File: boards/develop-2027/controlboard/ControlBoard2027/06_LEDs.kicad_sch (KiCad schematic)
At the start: 12 parts, among them U7 74AHCT125

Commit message: changes
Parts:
- added C51: 22uF, symbol Device:C
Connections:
- net +5V: now also C51.1
- net GND: now also C51.2
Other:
- note added: "LEVEL SHIFTER vs DOTSTAR RATE - checked, it works (design review asked). U7 = SN74AHCT125 quad buffer, tpd ~6-10 ns at 5V, rated well past 100 MHz. The design doc prescales the DotStar SPI to 7.815 Mbit/s (12 MHz is the APA102 ceiling). one bit at 7.815 MHz = 128 ns tpd 10 ns = 8% of a bit -> nowhere near the limit. VERDICT: fine. 3.3V INPUT SIDE - why the part is AHCT, not AHC: AHCT has TTL inpu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"

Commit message: post design review changes
post design review changes
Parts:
- added R66, R67: 100k, symbol Device:R
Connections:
- net GND: now also R66.2, R67.2
- net LED_SPI_MOSI: now also R67.1
- net LED_SPI_SCK: now also R66.1
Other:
- note added: "DOTSTAR LEVEL SHIFT U7 SN74AHCT125 on +5V, 3.3V in -> 5V out, tpd 6-10ns. BB-2020BGR-TRB VIH = 0.7 x VDD = 3.5V, so a shifter is needed. LED SPI (SPI2, TX only) = 3 Mbit/s in V0.3: bit = 333ns, tpd = 3% of a bit. LED max clock under 10MHz. Must be AHCT: VIH 2.0V (TTL). AHC needs 3.5V. Used: 1A p2 -> 1Y p3 CKI, 2A p5 -> 2Y p6 SDI, 1OE/2OE p1/p4 = GND. Spare gates 3/4: inputs p9/p12 = GND, OE p10/p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"
- note added: "ROUTING - DOTSTARS U7 -> D3 CLK/DATA short and routed together, over GND. LED-to-LED CO->CI and DO->DI as matched pairs. C40-C44 at each LED VDD pin. C51 where +5V enters the chain. LEDs in the 5-dot shell pattern."
- note removed: "LEVEL SHIFTER vs DOTSTAR RATE - checked, it works (design review asked). U7 = SN74AHCT125 quad buffer, tpd ~6-10 ns at 5V, rated well past 100 MHz. The design doc prescales the DotStar SPI to 7.815 Mbit/s (12 MHz is the APA102 ceiling). one bit at 7.815 MHz = 128 ns tpd 10 ns = 8% of a bit -> nowhere near the limit. VERDICT: fine. 3.3V INPUT SIDE - why the part is AHCT, not AHC: AHCT has TTL inpu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"

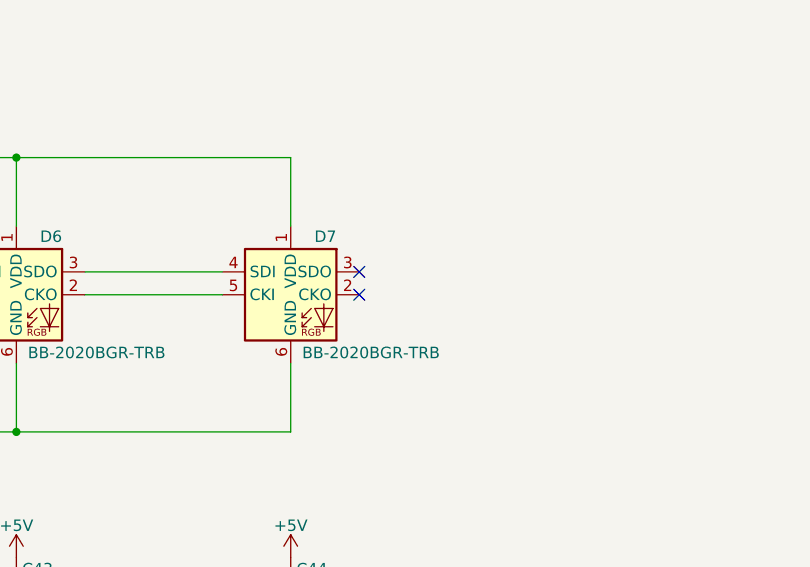
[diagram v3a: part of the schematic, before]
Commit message: added comments. Grouped submodules in ways that make more sense
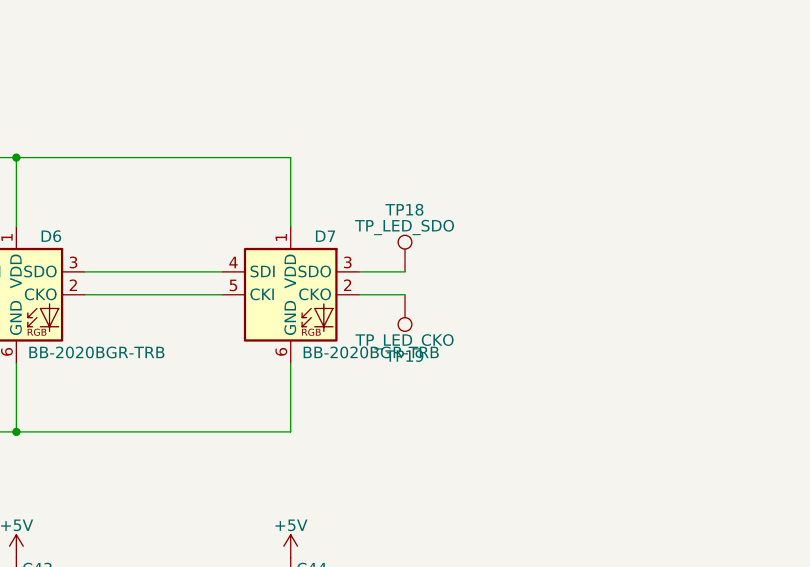
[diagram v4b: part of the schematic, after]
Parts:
- added TP18: TP_LED_SDO, symbol Connector:TestPoint
- added TP19: TP_LED_CKO, symbol Connector:TestPoint
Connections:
- net at D7.2 (CKO): now also TP19.1
- net at D7.3 (SDO): now also TP18.1
- no-connect marks 4 -> 2

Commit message: fixed minor errors
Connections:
- net +5V renamed +5V_PB
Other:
- note added: "DOTSTAR LEVEL SHIFT Power: +5V_PB (powerboard only). The LEDs and U7 are unpowered on USB, so a USB-only board never carries LED current. U7 inputs are rated -0.5 to 7V regardless of VCC and leak +/-1uA at VCC = 0V (SCLS264R), so 3.3V MCU drive is safe while U7 is off. U7 SN74AHCT125, 3.3V in -> 5V out, tpd 6.5ns max at 15pF (SCLS264R). BB-2020BGR-TRB VIH = 0.7 x VDD = 3.5V, so a shifter is neede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"
- note added: "ROUTING - DOTSTARS U7 -> D3 CLK/DATA short and routed together, over GND. LED-to-LED CO->CI and DO->DI as matched pairs. C40-C44 at each LED VDD pin. C51 where +5V_PB enters the chain. LEDs in the 5-dot shell pattern."
- note removed: "DOTSTAR LEVEL SHIFT U7 SN74AHCT125 on +5V, 3.3V in -> 5V out, tpd 6-10ns. BB-2020BGR-TRB VIH = 0.7 x VDD = 3.5V, so a shifter is needed. LED SPI (SPI2, TX only) = 3 Mbit/s in V0.3: bit = 333ns, tpd = 3% of a bit. LED max clock under 10MHz. Must be AHCT: VIH 2.0V (TTL). AHC needs 3.5V. Used: 1A p2 -> 1Y p3 CKI, 2A p5 -> 2Y p6 SDI, 1OE/2OE p1/p4 = GND. Spare gates 3/4: inputs p9/p12 = GND, OE p10/p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"
- note removed: "ROUTING - DOTSTARS U7 -> D3 CLK/DATA short and routed together, over GND. LED-to-LED CO->CI and DO->DI as matched pairs. C40-C44 at each LED VDD pin. C51 where +5V enters the chain. LEDs in the 5-dot shell pattern."

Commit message: Updated comments. Claude did an audit. Take it with huge grains of salt
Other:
- note added: "DOTSTAR LEVEL SHIFT The LEDs need a 5V-level logic high, so U7 (AHCT, TTL inputs) shifts the 3.3V SPI. Powered from +5V_PB: the LEDs never load USB, and U7 inputs are safe while unpowered. Used: 1A p2 -> 1Y p3 CKI, 2A p5 -> 2Y p6 SDI, 1OE/2OE p1/p4 = GND. Spare gates 3/4: inputs p9/p12 = GND, OE p10/p13 = +5V_PB (off), outputs p8/p11 open. R66/R67 hold the inputs low while the MCU pins float at r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"
- note removed: "DOTSTAR LEVEL SHIFT Power: +5V_PB (powerboard only). The LEDs and U7 are unpowered on USB, so a USB-only board never carries LED current. U7 inputs are rated -0.5 to 7V regardless of VCC and leak +/-1uA at VCC = 0V (SCLS264R), so 3.3V MCU drive is safe while U7 is off. U7 SN74AHCT125, 3.3V in -> 5V out, tpd 6.5ns max at 15pF (SCLS264R). BB-2020BGR-TRB VIH = 0.7 x VDD = 3.5V, so a shifter is neede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"
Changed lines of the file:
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@@
     (effects (font (size 1.27 1.27) (bold yes) (color 255 0 0 1)) (justify left bottom))
   )
-  (text "DOTSTAR LEVEL SHIFT\nPower: +5V_PB (powerboard only). The LEDs and U7 are unpowered on USB, so a USB-only\n  board never carries LED current. U7 inputs are rated -0.5 to 7V regardless of VCC and\n  leak +/-1uA at VCC = 0V (SCLS264R), so 3.3V MCU drive is safe while U7 is off.\nU7 SN74AHCT125, 3.3V in -> 5V out, tpd 6.5ns max at 15pF (SCLS264R).\nBB-2020BGR-TRB VIH = 0.7 x VDD = 3.5V, so a shifter is needed.\nLED SPI (SPI2, TX only) = 3 Mbit/s in V0.3:\n   bit = 333ns, tpd = 2% of a bit. LED clock 15MHz abs, under 10MHz operating (p6).\nMust be AHCT: VIH 2.0V (TTL). AHC needs 3.5V.\nUsed: 1A p2 -> 1Y p3 CKI, 2A p5 -> 2Y p6 SDI, 1OE/2OE p1/p4 = GND.\nSpare gates 3/4: inputs p9/p12 = GND, OE p10/p13 = +5V_PB (off), outputs p8/p11 open.\nLED power-on state is not specified: firmware sends an all-off frame first.\n!! Default KiCad APA102-2020 footprint does NOT fit this LED -\n   make one from the BB-2020BGR-TRB land pattern.\n\nDECOUPLING\n   C45 100nF at U7.\n   C40-C44 100nF, one per LED (D3-D7).\n   C51 22uF bulk, >= 10V X5R/X7R. Up to 0.5W per LED (p3): 500mA for 5 LEDs."
+  (text "DOTSTAR LEVEL SHIFT\nThe LEDs need a 5V-level logic high, so U7 (AHCT, TTL inputs) shifts the 3.3V SPI.\nPowered from +5V_PB: the LEDs never load USB, and U7 inputs are safe while unpowered.\nUsed: 1A p2 -> 1Y p3 CKI, 2A p5 -> 2Y p6 SDI, 1OE/2OE p1/p4 = GND.\nSpare gates 3/4: inputs p9/p12 = GND, OE p10/p13 = +5V_PB (off), outputs p8/p11 open.\nR66/R67 hold the inputs low while the MCU pins float at reset.\nLED power-on state is undefined: firmware sends an all-off frame first.\n!! Default KiCad APA102-2020 footprint does NOT fit this LED (C1).\nC45 at U7, C40-C44 one per LED, C51 bulk where +5V_PB enters.\nDESIGN_NOTES.md §10."
     (at 297.18 252.73 0)
     (effects (font (size 1.27 1.27)) (justify left bottom))

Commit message: boxing goes brrr
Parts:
- U7: MPN (none) -> TI SN74AHCT125PWR
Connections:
- net +5V_PB renamed +5V
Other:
- note added: "DOTSTAR CHAIN D3-D7 AND DECOUPLING"
- note added: "DOTSTAR LEVEL SHIFT The LEDs need a 5V-level logic high, so U7 (AHCT, TTL inputs) shifts the 3.3V SPI. LEDs and U7 run from +5V (mux output), so they also work on USB. Firmware caps LED current: ~250mA on the powerboard (F2 budget), ~100mA on USB (F1). Used: 1A p2 -> 1Y p3 CKI, 2A p5 -> 2Y p6 SDI, 1OE/2OE p1/p4 = GND. Spare gates 3/4: inputs p9/p12 = GND, OE p10/p13 = +5V (off), outputs p8/p11 op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"
- note added: "LEVEL SHIFT U7 (3.3V SPI TO 5V)"
- note added: "ROUTING - DOTSTARS U7 -> D3 CLK/DATA short and routed together, over GND. LED-to-LED CO->CI and DO->DI as matched pairs. C40-C44 at each LED VDD pin. C51 where +5V enters the chain. LEDs in the 5-dot shell pattern."
- note added: "U7 SPARE GATES"
- note removed: "DOTSTAR LEVEL SHIFT The LEDs need a 5V-level logic high, so U7 (AHCT, TTL inputs) shifts the 3.3V SPI. Powered from +5V_PB: the LEDs never load USB, and U7 inputs are safe while unpowered. Used: 1A p2 -> 1Y p3 CKI, 2A p5 -> 2Y p6 SDI, 1OE/2OE p1/p4 = GND. Spare gates 3/4: inputs p9/p12 = GND, OE p10/p13 = +5V_PB (off), outputs p8/p11 open. R66/R67 hold the inputs low while the MCU pins float at r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"
- note removed: "ROUTING - DOTSTARS U7 -> D3 CLK/DATA short and routed together, over GND. LED-to-LED CO->CI and DO->DI as matched pairs. C40-C44 at each LED VDD pin. C51 where +5V_PB enters the chain. LEDs in the 5-dot shell pattern."

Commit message: updated schematics based on feedback
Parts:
- added TP20: LED_SDI_IN, TestPoint:TestPoint_Pad_D1.0mm, symbol Connector:TestPoint
- added TP21: LED_CKI_IN, TestPoint:TestPoint_Pad_D1.0mm, symbol Connector:TestPoint
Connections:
- net at D3.5 (CKI), U7.3: now also TP21.1
- net at D3.4 (SDI), U7.6: now also TP20.1
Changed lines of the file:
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@@
 		(color 0 0 0 0)
 	)
+	(junction
+		(at 137.16 177.8)
+		(diameter 0)
+	)
+	(junction
+		(at 137.16 180.34)
+		(diameter 0)
+	)
 	(no_connect
 		(at 93.98 232.41)
@@
 		)
 	)
+	(text "ROUTING - DOTSTARS\nU7 -> D3 CLK/DATA short and routed together, over GND.\nLED-to-LED CO->CI and DO->DI as matched pairs.\nC40-C44 at each LED VDD pin. C51 where +5V enters the chain.\nLEDs in the 5-dot shell pattern."
+		(at 199.39 149.86 0)
+		(effects
+			(font
+				(size 1.27 1.27)
+				(bold yes)
+				(color 255 0 0 1)
+			)
+			(justify left bottom)
+		)
+	)
+	(text "DOTSTAR LEVEL SHIFT\nThe LEDs need a 5V-level logic high, so U7 (AHCT, TTL inputs) shifts the 3.3V SPI.\nLEDs and U7 run from +5V (mux output), so they also work on USB.\nFirmware caps LED current: ~250mA on the powerboard (F2 budget), ~100mA on USB (F1).\nUsed: 1A p2 -> 1Y p3 CKI, 2A p5 -> 2Y p6 SDI, 1OE/2OE p1/p4 = GND.\nSpare gates 3/4: inputs p9/p12 = GND, OE p10/p13 = +5V (off), outputs p8/p11 open.\nR66/R67 hold the inputs low while the MCU pins float at reset.\nLED power-on state is undefined: firmware sends an all-off frame first.\n!! Default KiCad APA102-2020 footprint does NOT fit this LED (C1).\nC45 at U7, C40-C44 one per LED, C51 bulk where +5V enters.\nDESIGN_NOTES.md §10."
+		(at 297.18 252.73 0)
+		(effects
+			(font
+				(size 1.27 1.27)
+			)
+			(justify left bottom)
+		)
+	)
+	(text "LEVEL SHIFT U7 (3.3V SPI TO 5V)"
+		(at 50.8 95.25 0)
+		(effects
+			(font
+				(size 2 2)
+				(thickness 0.4)
+				(bold yes)
+				(color 0 0 132 1)
+			)
+			(justify left bottom)
+		)
+	)
+	(text "DOTSTAR CHAIN D3-D7 AND DECOUPLING"
+		(at 116.84 139.7 0)
+		(effects
+			(font
+				(size 2 2)
+				(thickness 0.4)
+				(bold yes)
+				(color 0 0 132 1)
+			)
+			(justify left bottom)
+		)
+	)
+	(text "U7 SPARE GATES"
+		(at 40.64 229.87 0)
+		(effects
+			(font
+				(size 2 2)
+				(thickness 0.4)
+				(bold yes)
+				(color 0 0 132 1)
+			)
+			(justify left bottom)
+		)
+	)
 	(hierarchical_label "LED_SPI_MOSI"
 		(shape input)
@@
 		)
 	)
-  (text "ROUTING - DOTSTARS\nU7 -> D3 CLK/DATA short and routed together, over GND.\nLED-to-LED CO->CI and DO->DI as matched pairs.\nC40-C44 at each LED VDD pin. C51 where +5V enters the chain.\nLEDs in the 5-dot shell pattern."
-    (at 199.39 149.86 0)
-    (effects (font (size 1.27 1.27) (bold yes) (color 255 0 0 1)) (justify left bottom))
-  )
-  (text "DOTSTAR LEVEL SHIFT\nThe LEDs need a 5V-level logic high, so U7 (AHCT, TTL inputs) shifts the 3.3V SPI.\nLEDs and U7 run from +5V (mux output), so they also work on USB.\nFirmware caps LED current: ~250mA on the powerboard (F2 budget), ~100mA on USB (F1).\nUsed: 1A p2 -> 1Y p3 CKI, 2A p5 -> 2Y p6 SDI, 1OE/2OE p1/p4 = GND.\nSpare gates 3/4: inputs p9/p12 = GND, OE p10/p13 = +5V (off), outputs p8/p11 open.\nR66/R67 hold the inputs low while the MCU pins float at reset.\nLED power-on state is undefined: firmware sends an all-off frame first.\n!! Default KiCad APA102-2020 footprint does NOT fit this LED (C1).\nC45 at U7, C40-C44 one per LED, C51 bulk where +5V enters.\nDESIGN_NOTES.md §10."
-    (at 297.18 252.73 0)
-    (effects (font (size 1.27 1.27)) (justify left bottom))
-  )
-  (text "LEVEL SHIFT U7 (3.3V SPI TO 5V)"
-    (at 50.8 95.25 0)
-    (effects (font (size 2 2) (thickness 0.4) (bold yes) (color 0 0 132 1)) (justify left bottom))
-  )
-  (text "DOTSTAR CHAIN D3-D7 AND DECOUPLING"
-    (at 116.84 139.7 0)
-    (effects (font (size 2 2) (thickness 0.4) (bold yes) (color 0 0 132 1)) (justify left bottom))
-  )
-  (text "U7 SPARE GATES"
-    (at 40.64 229.87 0)
-    (effects (font (size 2 2) (thickness 0.4) (bold yes) (color 0 0 132 1)) (justify left bottom))
-  )
 	(symbol
 		(lib_id "Device:R")
@@
 			)
 		)
+		(property "MPN" "TI SN74AHCT125PWR"
+			(at 86.36 180.34 0)
+			(hide yes)
+			(effects
+				(font
+					(size 1.27 1.27)
+				)
+			)
+		)
 		(body_style 1)
 		(in_pos_files yes)
@@
 			)
 		)
-		(property "MPN" "TI SN74AHCT125PWR"
-			(at 86.36 180.34 0)
-			(hide yes)
-			(effects
-				(font
-					(size 1.27 1.27)
-				)
-			)
-		))
+	)
 	(symbol
 		(lib_id "74xx:74AHCT125")
@@
 			)
 		)
+		(property "MPN" "TI SN74AHCT125PWR"
+			(at 86.36 157.48 0)
+			(hide yes)
+			(effects
+				(font
+					(size 1.27 1.27)
+				)
+			)
+		)
 		(body_style 1)
 		(in_pos_files yes)
@@
 			)
 		)
-		(property "MPN" "TI SN74AHCT125PWR"
-			(at 86.36 157.48 0)
-			(hide yes)
-			(effects
-				(font
-					(size 1.27 1.27)
-				)
-			)
-		))
+	)
 	(symbol
 		(lib_id "power:GND")
@@
 			)
 		)
+		(property "MPN" "TI SN74AHCT125PWR"
+			(at 86.36 232.41 0)
+			(hide yes)
+			(effects
+				(font
+					(size 1.27 1.27)
+				)
+			)
+		)
 		(body_style 1)
 		(in_pos_files yes)
@@
 			)
 		)
-		(property "MPN" "TI SN74AHCT125PWR"
-			(at 86.36 232.41 0)
-			(hide yes)
-			(effects
-				(font
-					(size 1.27 1.27)
-				)
-			)
-		))
+	)
 	(symbol
 		(lib_id "power:GND")
@@
 			)
 		)
+		(property "MPN" "TI SN74AHCT125PWR"
+			(at 86.36 120.65 0)
+			(hide yes)
+			(effects
+				(font
+					(size 1.27 1.27)
+				)
+			)
+		)
 		(body_style 1)
 		(in_pos_files yes)
@@
 			)
 		)
-		(property "MPN" "TI SN74AHCT125PWR"
-			(at 86.36 120.65 0)
-			(hide yes)
-			(effects
-				(font
-					(size 1.27 1.27)
-				)
-			)
-		))
+	)
 	(symbol
 		(lib_id "Device:C")
@@
 			)
 		)
+		(property "MPN" "TI SN74AHCT125PWR"
+			(at 152.4 232.41 0)
+			(hide yes)
+			(effects
+				(font
+					(size 1.27 1.27)
+				)
+			)
+		)
 		(body_style 1)
 		(in_pos_files yes)
@@
 			)
 		)
-		(property "MPN" "TI SN74AHCT125PWR"
-			(at 152.4 232.41 0)
-			(hide yes)
-			(effects
-				(font
-					(size 1.27 1.27)
-				)
-			)
-		))
+	)
 	(symbol
 		(lib_id "power:GND")
@@
 					(unit 1)
 				)
+			)
+		)
+	)
+	(symbol
+		(lib_id "Connector:TestPoint")
+		(at 137.16 177.8 0)
+		(unit 1)
+		(in_bom yes)
+		(on_board yes)
+		(dnp no)
+		(property "Reference" "TP20"
+			(at 137.16 170.942 0)
+			(effects
+				(font
+					(size 1.27 1.27)
+				)
+			)
+		)
+		(property "Value" "LED_SDI_IN"
+			(at 137.16 172.72 0)
+			(effects
+				(font
+					(size 1.27 1.27)
+				)
+			)
+		)
+		(property "Footprint" "TestPoint:TestPoint_Pad_D1.0mm"
+			(at 137.16 177.8 0)
+			(hide yes)
+			(effects
+				(font
+					(size 1.27 1.27)
+				)
+			)
+		)
+		(property "Datasheet" "https://americanbrightled.com/products/rgb-ic-led-components/"
+			(at 137.16 177.8 0)
+			(hide yes)
+			(effects
+				(font
+					(size 1.27 1.27)
+				)
+			)
+		)
+		(property "Description" "Beginning of LED chain: D3 SDI pin 4 after U7 level shifting. Compare against TP18 (D7 SDO)."
+			(at 137.16 177.8 0)
+			(hide yes)
+			(effects
+				(font
+					(size 1.27 1.27)
+				)
+			)
+		)
+		(instances
+			(project "ControlBoard2027"
+				(path "/2be89789-dd04-494d-960d-2531c7ce8a2f/ee62a278-a94c-4411-ba4b-a0279340f73e"
+					(reference "TP20")
+					(unit 1)
+				)
+			)
+		)
+	)
+	(symbol
+		(lib_id "Connector:TestPoint")
+		(at 137.16 180.34 180)
+		(unit 1)
+		(in_bom yes)
+		(on_board yes)
+		(dnp no)
+		(property "Reference" "TP21"
+			(at 137.16 187.198 0)
+			(effects
+				(font
+					(size 1.27 1.27)
+				)
+			)
+		)
+		(property "Value" "LED_CKI_IN"
+			(at 137.16 185.42 0)
+			(effects
+				(font
+					(size 1.27 1.27)
+				)
+			)
+		)
+		(property "Footprint" "TestPoint:TestPoint_Pad_D1.0mm"
+			(at 137.16 180.34 0)
+			(hide yes)
+			(effects
+				(font
+					(size 1.27 1.27)
+				)
+			)
+		)
+		(property "Datasheet" "https://americanbrightled.com/products/rgb-ic-led-components/"
+			(at 137.16 180.34 0)
+			(hide yes)
+			(effects
+				(font
+					(size 1.27 1.27)
+				)
+			)
+		)
+		(property "Description" "Beginning of LED chain: D3 CKI pin 5 after U7 level shifting. Compare against TP19 (D7 CKO)."
+			(at 137.16 180.34 0)
+			(hide yes)
+			(effects
+				(font
+					(size 1.27 1.27)
+				)
+			)
+		)
+		(instances
+			(project "ControlBoard2027"
+				(path "/2be89789-dd04-494d-960d-2531c7ce8a2f/ee62a278-a94c-4411-ba4b-a0279340f73e"
+					(reference "TP21")
+					(unit 1)
+				)
